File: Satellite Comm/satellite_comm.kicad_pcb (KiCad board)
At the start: 2 copper layers, 139.7 x 100.3 mm, 10 parts, among them J1 RockBlock Connector, J2 PC104_40Pin_2.54mm-WhitworthS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, U1 SAM-M8Q

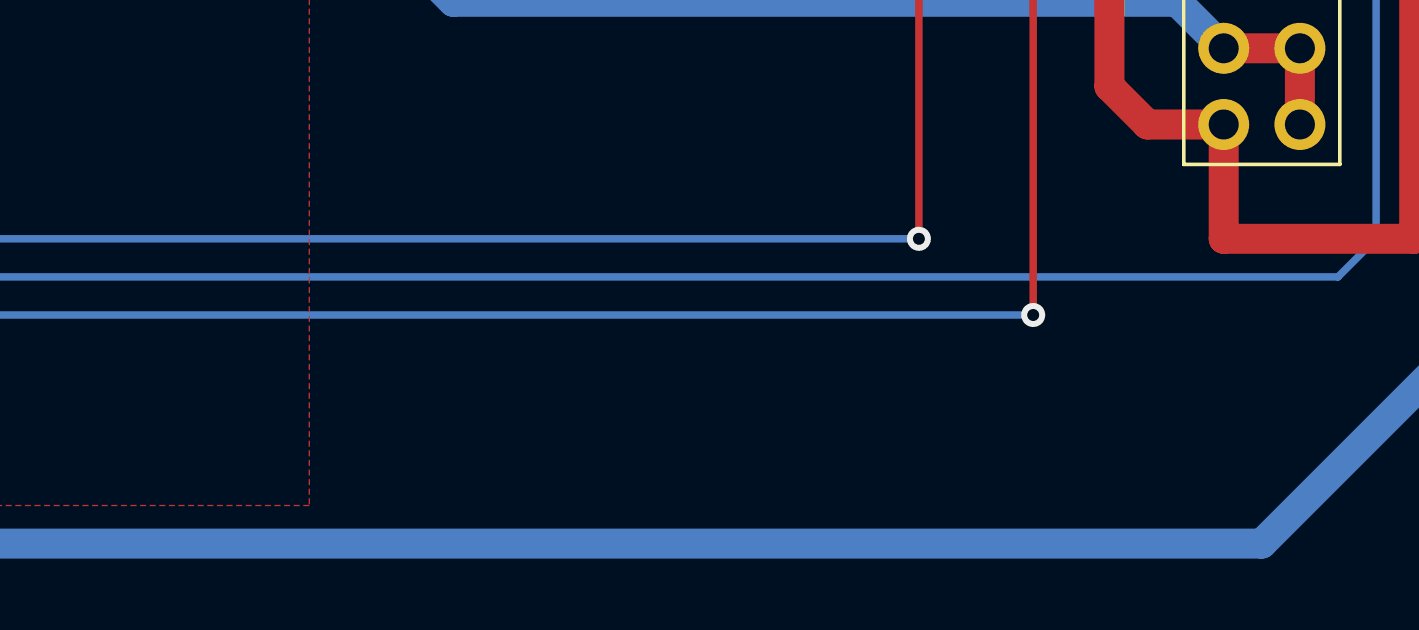
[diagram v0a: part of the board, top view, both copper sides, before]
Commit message: Added one more ground track
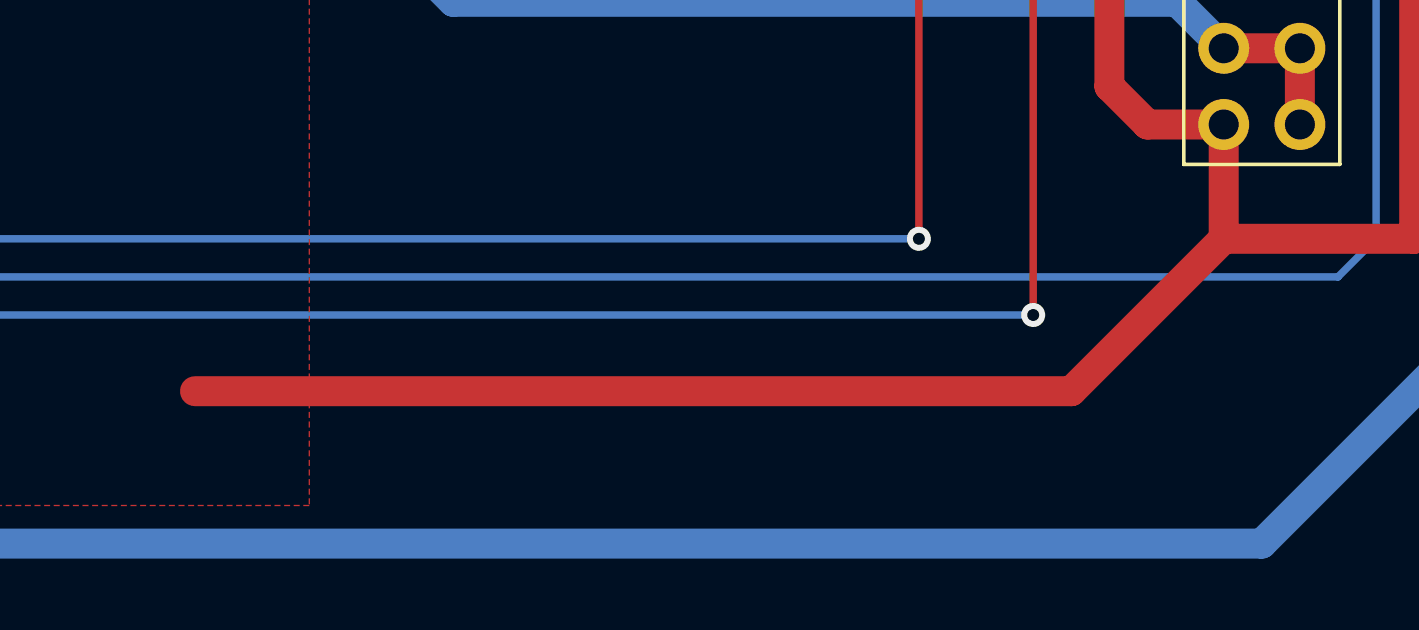
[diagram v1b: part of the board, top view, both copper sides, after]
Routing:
- net GND: track 233.4 -> 269.8 mm
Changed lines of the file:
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@@
     (thickness 1.6)
     (drawings 25)
-    (tracks 176)
+    (tracks 178)
     (zones 0)
     (modules 10)
@@
   )
   (setup
-    (last_trace_width 0.25)
+    (last_trace_width 1)
     (user_trace_width 1)
     (trace_clearance 0.2)
@@
   (segment (start 33.02 82.55) (end 33.02 85.09) (width 1) (layer F.Cu) (net 1))
   (segment (start 33.745 81.825) (end 33.02 82.55) (width 1) (layer F.Cu) (net 1))
+  (segment (start 154.94 104.14) (end 149.86 109.22) (width 1) (layer F.Cu) (net 1))
+  (segment (start 149.86 109.22) (end 120.65 109.22) (width 1) (layer F.Cu) (net 1))
   (via (at 41.91 80.01) (size 0.8) (drill 0.4) (layers F.Cu B.Cu) (net 2))
   (segment (start 162.56 57.15) (end 157.48 52.07) (width 1) (layer B.Cu) (net 2))

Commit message: minor, unimportant updates (deleting iridium_ri label since we aren't connecting that)
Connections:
- net /IRIDIUM_RI renamed Net-(J1-Pad6)

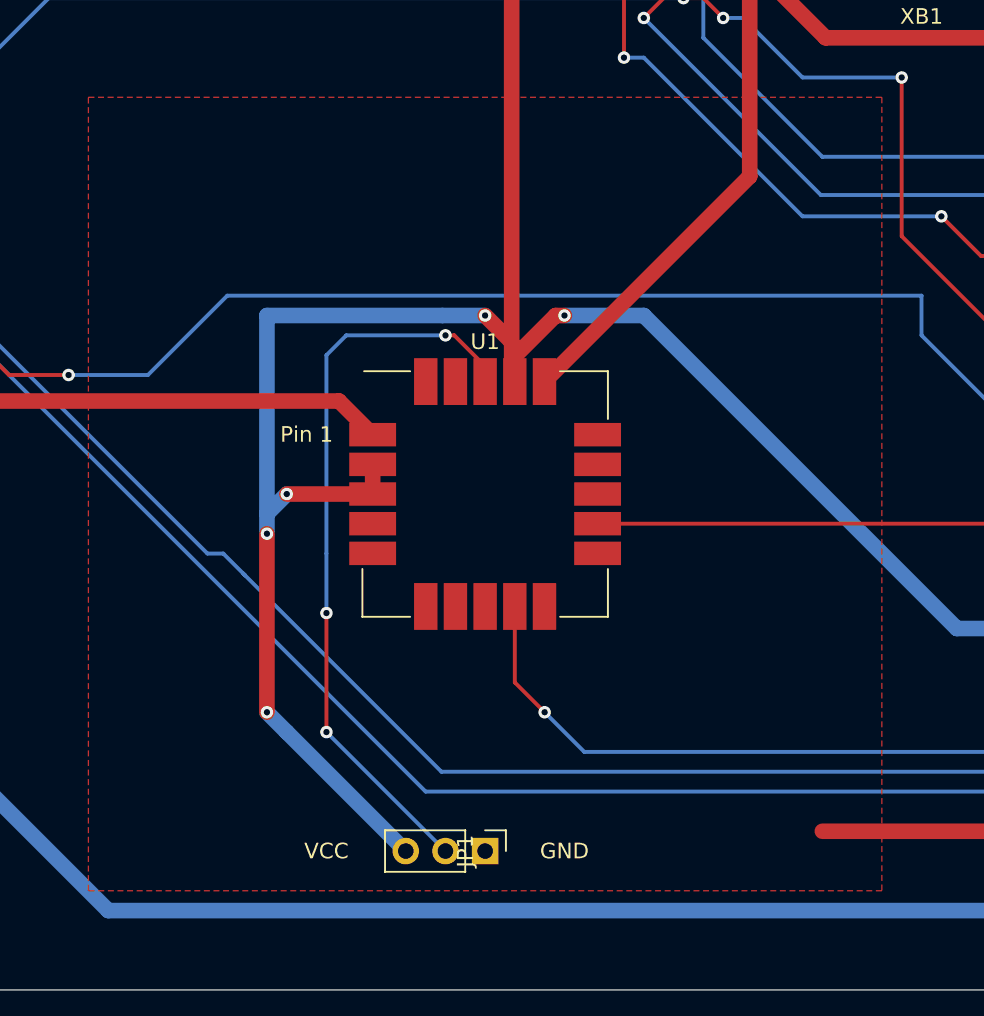
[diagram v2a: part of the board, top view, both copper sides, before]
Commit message: Update satellite_comm.kicad_pcb
Add bottom ground plane. Connect ground planes with via mesh.
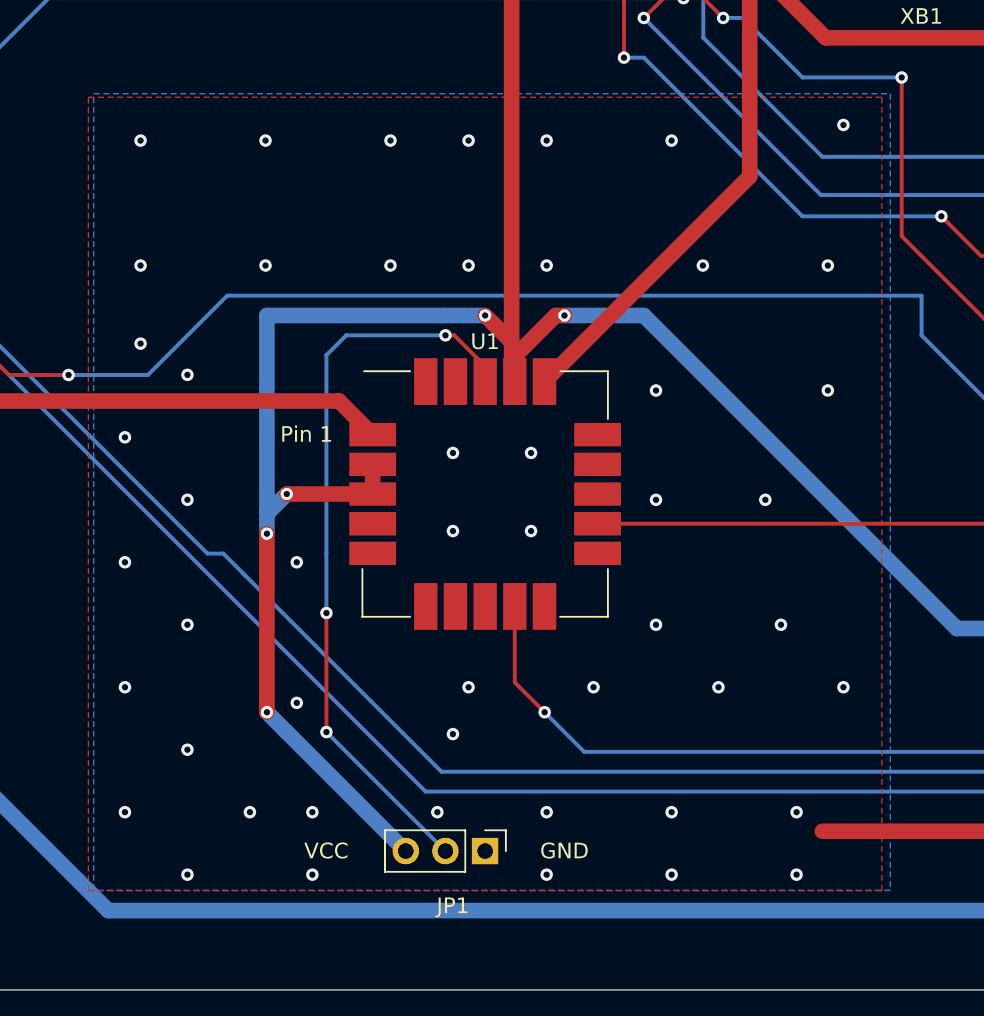
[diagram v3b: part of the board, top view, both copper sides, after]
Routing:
- net GND: vias 0 -> 51
- added copper zone on B.Cu, net GND
